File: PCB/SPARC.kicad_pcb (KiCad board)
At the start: 4 copper layers, 40 x 40 mm, 58 parts, among them J1 Conn_Coaxial_Power, J2 Conn_Coaxial_Power, J3 Conn_01x06_Female, J4 Conn_01x03_Female, J5 Conn_01x03_Female, J6 Conn_01x06_Female, U1 HV2621, U2 HV2621

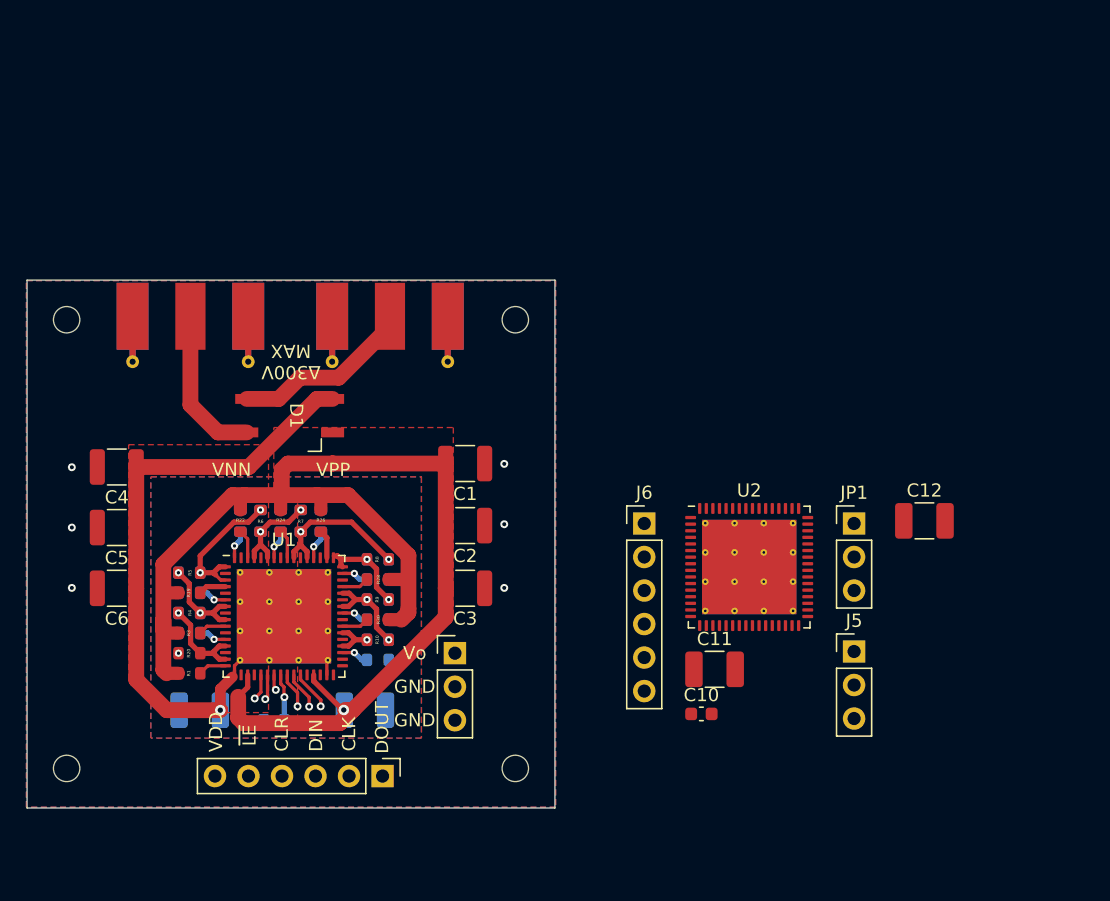
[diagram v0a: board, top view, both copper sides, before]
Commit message: Worked on adding second channel
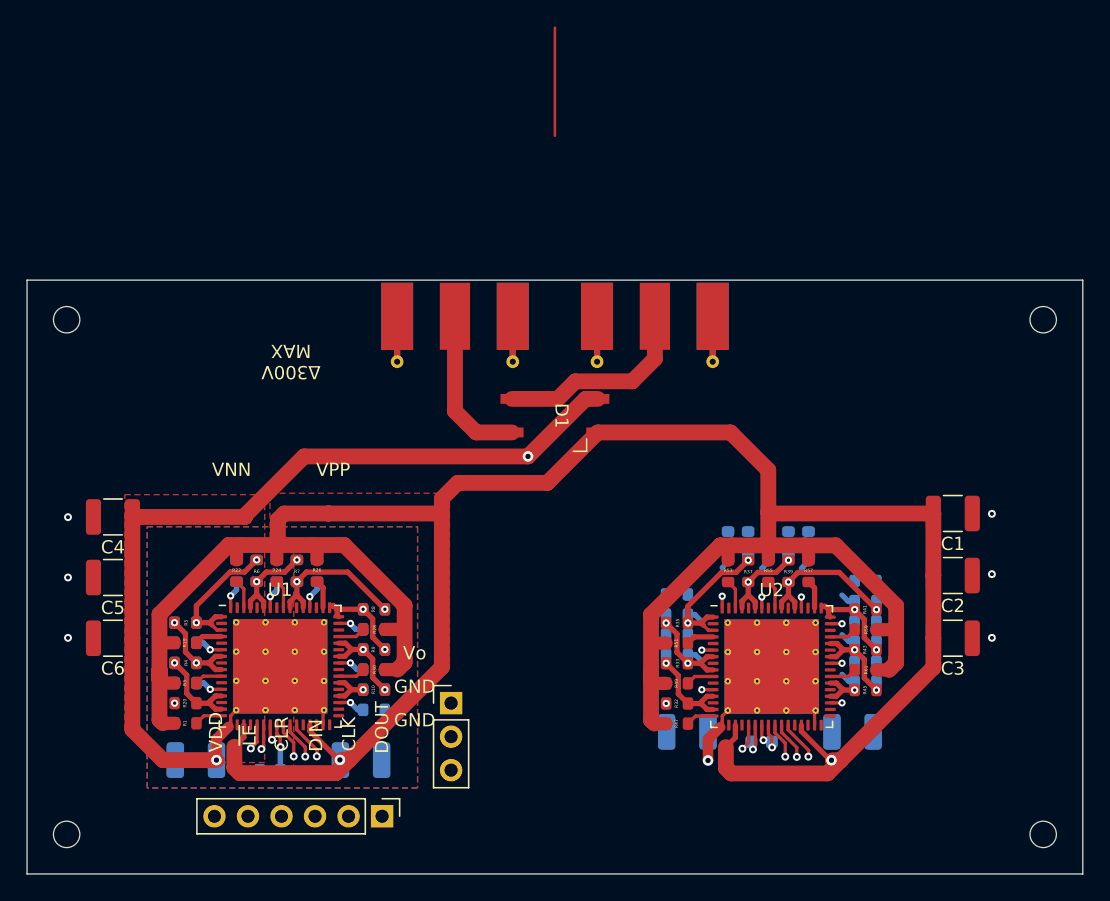
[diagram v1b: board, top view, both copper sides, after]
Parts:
- removed J5: Conn_01x03_Female, Connector_PinHeader_2.54mm:PinHeader_1x03_P2.54mm_Vertical
- removed J6: Conn_01x06_Female, Connector_PinHeader_2.54mm:PinHeader_1x06_P2.54mm_Vertical
- removed JP1: Jumper_3_Open, Connector_PinHeader_2.54mm:PinHeader_1x03_P2.54mm_Vertical
- added R32: ${2R}, grad_kicad_foot:R_0603_1608Metric_small_silk, F.Cu at (132.7, 76.7)
- added R33: ${2R}, grad_kicad_foot:R_0603_1608Metric_small_silk, F.Cu at (132.7, 73.7)
- added R34: ${2R}, grad_kicad_foot:R_0603_1608Metric_small_silk, B.Cu at (132.6, 71.5)
- added R35: ${2R}, grad_kicad_foot:R_0603_1608Metric_small_silk, F.Cu at (132.7, 70.6)
- added R36: ${2R}, grad_kicad_foot:R_0603_1608Metric_small_silk, B.Cu at (132.6, 68.4)
- added R37: ${2R}, grad_kicad_foot:R_0603_1608Metric_small_silk, F.Cu at (138.0, 66.7)
- added R38: ${2R}, grad_kicad_foot:R_0603_1608Metric_small_silk, B.Cu at (138.0, 64.5)
- added R39: ${2R}, grad_kicad_foot:R_0603_1608Metric_small_silk, F.Cu at (141.1, 66.7)
- added R40: ${2R}, grad_kicad_foot:R_0603_1608Metric_small_silk, B.Cu at (141.1, 64.5)
- added R41: ${2R}, grad_kicad_foot:R_0603_1608Metric_small_silk, F.Cu at (146.9, 69.6)
- added R42: ${2R}, grad_kicad_foot:R_0603_1608Metric_small_silk, B.Cu at (146.9, 67.4)
- added R43: ${2R}, grad_kicad_foot:R_0603_1608Metric_small_silk, F.Cu at (146.9, 72.6)
- added R44: ${2R}, grad_kicad_foot:R_0603_1608Metric_small_silk, B.Cu at (146.9, 70.5)
- added R45: ${2R}, grad_kicad_foot:R_0603_1608Metric_small_silk, F.Cu at (146.9, 75.7)
- added R46: ${2R}, grad_kicad_foot:R_0603_1608Metric_small_silk, B.Cu at (146.9, 73.5)
- added R47: ${2R}, grad_kicad_foot:R_0603_1608Metric_small_silk, F.Cu at (132.7, 78.2)
- added R48: ${2R}, grad_kicad_foot:R_0603_1608Metric_small_silk, B.Cu at (132.6, 73.0)
- added R49: ${2R}, grad_kicad_foot:R_0603_1608Metric_small_silk, F.Cu at (132.7, 75.2)
- added R50: ${2R}, grad_kicad_foot:R_0603_1608Metric_small_silk, B.Cu at (132.6, 70.0)
- added R51: ${2R}, grad_kicad_foot:R_0603_1608Metric_small_silk, F.Cu at (132.7, 72.1)
- added R52: ${2R}, grad_kicad_foot:R_0603_1608Metric_small_silk, B.Cu at (136.5, 64.5)
- added R53: ${2R}, grad_kicad_foot:R_0603_1608Metric_small_silk, F.Cu at (136.5, 66.7)
- added R54: ${2R}, grad_kicad_foot:R_0603_1608Metric_small_silk, B.Cu at (139.6, 64.5)
- added R55: ${2R}, grad_kicad_foot:R_0603_1608Metric_small_silk, F.Cu at (139.6, 66.7)
- added R56: ${2R}, grad_kicad_foot:R_0603_1608Metric_small_silk, B.Cu at (142.6, 64.5)
- added R57: ${2R}, grad_kicad_foot:R_0603_1608Metric_small_silk, F.Cu at (142.6, 66.7)
- added R58: ${2R}, grad_kicad_foot:R_0603_1608Metric_small_silk, B.Cu at (146.9, 69.0)
- added R59: ${2R}, grad_kicad_foot:R_0603_1608Metric_small_silk, F.Cu at (146.9, 71.1)
- added R60: ${2R}, grad_kicad_foot:R_0603_1608Metric_small_silk, B.Cu at (146.9, 72.0)
- added R61: ${2R}, grad_kicad_foot:R_0603_1608Metric_small_silk, F.Cu at (146.9, 74.2)
- added R62: ${2R}, grad_kicad_foot:R_0603_1608Metric_small_silk, B.Cu at (146.9, 75.0)
- C10, C11, C12: moved to B.Cu
- moved REF** 40.3 mm to (160.4, 86.6)
- moved REF** 40.0 mm to (160.4, 47.6)
- moved C1 37.1 mm to (153.6, 62.3)
- moved C2 37.1 mm to (153.6, 67.0)
- moved C3 37.1 mm to (153.6, 71.8)
- moved D1 20.1 mm to (123.4, 54.9)
- moved J2 20.1 mm to (131.0, 49.1)
- moved J1 20.0 mm to (115.8, 49.1)
- moved C12 16.9 mm to (146.0, 78.9), turned to 180 degrees
- moved U2 7.73 mm to (139.8, 73.9)
- moved C11 5.17 mm to (133.4, 78.9)
- moved C10 5.03 mm to (139.1, 79.6), turned to 180 degrees
- moved REF** 5.00 mm to (86.4, 86.6)
- moved C7 3.80 mm to (108.7, 81.0)
- moved C8 3.80 mm to (101.8, 81.8)
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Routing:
- net /VPP: track 99.2 -> 238.2 mm, vias 1 -> 2
- net /VNN: track 46.0 -> 105.5 mm, vias 1 -> 3
- net /VDD: track 18.9 -> 34.7 mm, vias 1 -> 2
- net /VB4_1: track 0.00 -> 11.5 mm, vias 0 -> 2
- net /VB2_1: track 0.00 -> 10.5 mm, vias 0 -> 2
- net /~{LE_0}: track 10.8 -> 19.4 mm
- net /VB0_1: track 0.00 -> 7.38 mm, vias 0 -> 1
- net /VB3_1: track 0.00 -> 7.11 mm, vias 0 -> 2
- net /VB7_0: track 10.3 -> 17.4 mm
- net /VB1_1: track 0.00 -> 7.02 mm, vias 0 -> 2
- net /VB6_1: track 0.00 -> 6.98 mm, vias 0 -> 2
- net /VB5_1: track 0.00 -> 6.93 mm, vias 0 -> 2
- net /DOUT_0: track 10.1 -> 16.9 mm
- net /CLR_0: track 8.72 -> 14.8 mm
- net /DIN_0: track 8.55 -> 13.8 mm
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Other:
- board size 40 x 40 mm -> 80 x 45 mm

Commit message: Changed resistors and added jumpers
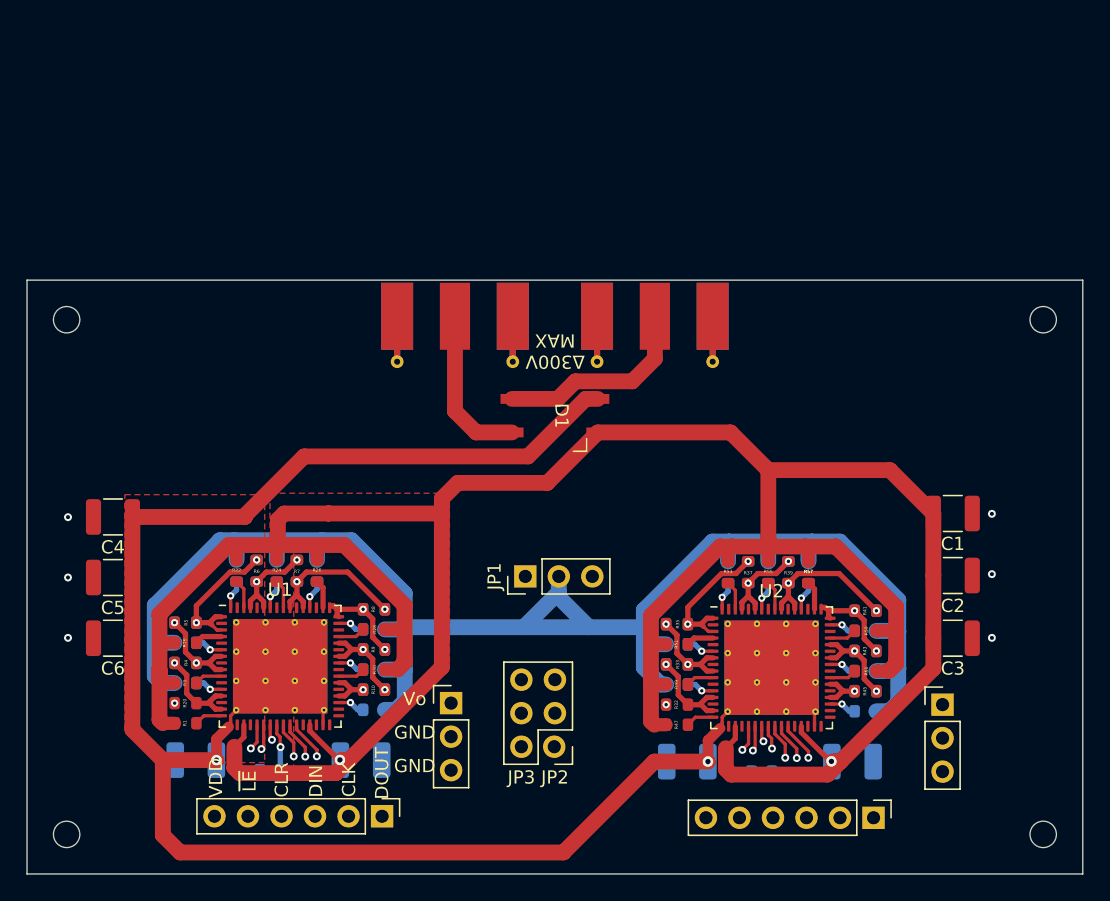
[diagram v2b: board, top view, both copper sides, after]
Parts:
- added J5: Conn_01x03_Female, Connector_PinHeader_2.54mm:PinHeader_1x03_P2.54mm_Vertical, F.Cu at (152.8, 76.8)
- added J6: Conn_01x06_Female, Connector_PinHeader_2.54mm:PinHeader_1x06_P2.54mm_Vertical, F.Cu at (147.5, 85.4)
- added JP1: Jumper_3_Open, Connector_PinHeader_2.54mm:PinHeader_1x03_P2.54mm_Vertical, F.Cu at (121.2, 67.1)
- added JP3 JP2: PinHeader_2x03_P2.54mm_Vertical, Connector_PinHeader_2.54mm:PinHeader_2x03_P2.54mm_Vertical, F.Cu at (123.4, 80.0)
- added R57: ${2R}, grad_kicad_foot:R_0603_1608Metric_small_silk, F.Cu at (142.6, 66.8)
- moved R46 2.25 mm to (146.9, 75.8)
- moved R62 2.25 mm to (146.9, 77.3)
- moved C10 2.25 mm to (139.1, 81.9)
- moved C11 2.25 mm to (133.4, 81.1)
- moved C12 2.25 mm to (146.0, 81.1)
- moved R34 2.25 mm to (132.6, 73.7)
- moved R36 2.25 mm to (132.6, 70.7)
- moved R38 2.25 mm to (138.0, 66.8)
- moved R40 2.25 mm to (141.1, 66.8)
- moved R42 2.25 mm to (146.9, 69.7)
- moved R44 2.25 mm to (146.9, 72.7)
- moved R48 2.25 mm to (132.6, 75.3)
- moved R50 2.25 mm to (132.6, 72.2)
- moved R52 2.25 mm to (136.5, 66.8)
- moved R54 2.25 mm to (139.6, 66.8)
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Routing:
- net /VL: track 0.00 -> 125.4 mm
- net /CLK_1: track 0.00 -> 20.1 mm
- net /VNN: track 105.5 -> 124.0 mm, vias 3 -> 2
- net /DIN_1: track 0.00 -> 13.7 mm
- net /~{LE_0}: track 19.4 -> 10.6 mm
- net /~{LE_1}: track 1.91 -> 10.7 mm
- net /VB7_0: track 17.4 -> 10.3 mm
- net /VB7_1: track 3.23 -> 10.3 mm
- net /DOUT_0: track 16.9 -> 9.86 mm
- net /DOUT_1: track 3.03 -> 9.86 mm
- net /CLR_0: track 14.8 -> 8.09 mm
- net /CLR_1: track 1.98 -> 8.09 mm
- net /DIN_0: track 13.8 -> 7.92 mm
- net /VPP: track 238.2 -> 233.2 mm
- removed copper zone on B.Cu, net GND
- removed copper zone on F.Cu, net GND
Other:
- board text removed: "VNN"
- board text removed: "VPP"

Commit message: Finished traces, finalized board
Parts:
- removed kibuzzard-63A22B4E: G***, kibuzzard-63A22B4E
- moved JP3 JP2 2.22 mm to (124.8, 81.7)
- moved JP1 0.52 mm to (120.9, 66.7)
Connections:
- JP3 JP2 pad 1: /CLK_1 -> /DIN_1
- JP3 JP2 pad 2: /DIN_1 -> /CLK_1
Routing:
- net /VDD: track 35.2 -> 76.2 mm
- net /SRi_1: track 2.71 -> 34.9 mm
- net /CLK_0: track 8.77 -> 38.5 mm
- net /SRc_1: track 2.89 -> 23.2 mm
- net /DOUT_0: track 9.86 -> 28.9 mm
- net /VNN: track 124.0 -> 134.6 mm, vias 2 -> 3
- net /DIN_1: track 13.7 -> 22.5 mm
- net /CLK_1: track 20.1 -> 28.1 mm
- net /VL: track 125.4 -> 121.2 mm
- added copper zone on B.Cu, net /VL
- added copper zone on B.Cu, net GND
- added copper zone on F.Cu, net GND
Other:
- board text added: "2CH-HV-DAC"
- board text added: "Daisy-Chain"
- board text added: "Independent"
- board text added: "Original 1CH Design: Randy Palamar 2023 <palamar@ualberta.ca> 2CH Design: Kirk Rieberger 2023 <rieberg1@ualberta.ca>"
- board text added: "VPP/GND"
- board text added: "VPP/VNN"
- board text removed: "Randy Palamar 2023 <palamar@ualberta.ca>"

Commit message: Updated R20 & R32 connection
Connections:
- R20 pad 2: GND -> /VL
- R32 pad 2: GND -> /VL
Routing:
- net GND: vias 10 -> 8
- net /VL: vias 0 -> 2
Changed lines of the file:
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@@
       (net 55 "/VB0_0") (pintype "passive"))
     (pad "2" smd roundrect (at 0.825 0 180) (size 0.8 0.95) (layers "F.Cu" "F.Paste" "F.Mask") (roundrect_rratio 0.25)
-      (net 7 "GND") (pintype "passive"))
+      (net 54 "/VL") (pintype "passive"))
     (model "${KICAD6_3DMODEL_DIR}/Resistor_SMD.3dshapes/R_0603_1608Metric.wrl"
       (offset (xyz 0 0 0))
@@
       (net 72 "/VB0_1") (pintype "passive"))
     (pad "2" smd roundrect (at 0.825 0 180) (size 0.8 0.95) (layers "F.Cu" "F.Paste" "F.Mask") (roundrect_rratio 0.25)
-      (net 7 "GND") (pintype "passive"))
+      (net 54 "/VL") (pintype "passive"))
     (model "${KICAD6_3DMODEL_DIR}/Resistor_SMD.3dshapes/R_0603_1608Metric.wrl"
       (offset (xyz 0 0 0))
@@
   (gr_line (start 127 79.3) (end 127 82.5) (layer "F.SilkS") (width 0.2))
   (gr_line (start 123.1 64.5) (end 126.3 64.5) (layer "F.SilkS") (width 0.2))
-  (gr_rect (start 92.784 59.478769) (end 113.359 79.378769) (layer "Dwgs.User") (width 0.2) (fill none))
+  (gr_rect (start 83.43 44.61) (end 163.399 89.64) (layer "Dwgs.User") (width 0.2) (fill none))
   (gr_rect (start 83.4 44.628769) (end 163.4 89.628769) (layer "Edge.Cuts") (width 0.1) (fill none))
   (gr_text "2CH-HV-DAC" (at 99.1 47.8) (layer "B.SilkS")
@@
   (via (at 86.502682 71.735369) (size 0.6) (drill 0.3) (layers "F.Cu" "B.Cu") (free) (net 7))
   (via (at 156.513682 71.735369) (size 0.6) (drill 0.3) (layers "F.Cu" "B.Cu") (free) (net 7))
-  (via (at 131.827682 76.796) (size 0.55) (drill 0.25) (layers "F.Cu" "B.Cu") (net 7))
   (via (at 86.502682 67.163369) (size 0.6) (drill 0.3) (layers "F.Cu" "B.Cu") (free) (net 7))
   (via (at 156.513682 62.337369) (size 0.6) (drill 0.3) (layers "F.Cu" "B.Cu") (free) (net 7))
@@
   (via (at 156.513682 66.909369) (size 0.6) (drill 0.3) (layers "F.Cu" "B.Cu") (free) (net 7))
   (via (at 86.502682 62.591369) (size 0.6) (drill 0.3) (layers "F.Cu" "B.Cu") (free) (net 7))
-  (via (at 94.583682 76.6846) (size 0.55) (drill 0.25) (layers "F.Cu" "B.Cu") (net 7))
   (via (at 139.202682 79.574769) (size 0.6) (drill 0.3) (layers "F.Cu" "B.Cu") (free) (net 7))
   (segment (start 102.828682 78.3261) (end 102.828682 78.9046) (width 0.25) (layer "F.Cu") (net 8))
@@
   (segment (start 99.828682 69.4511) (end 99.828682 68.0306) (width 0.25) (layer "F.Cu") (net 53))
   (segment (start 99.828682 68.0306) (end 99.276682 67.4786) (width 0.25) (layer "F.Cu") (net 53))
+  (via (at 131.827682 76.796) (size 0.55) (drill 0.25) (layers "F.Cu" "B.Cu") (net 54))
+  (via (at 94.583682 76.6846) (size 0.55) (drill 0.25) (layers "F.Cu" "B.Cu") (net 54))
   (segment (start 130.14 73.98) (end 131.43 75.27) (width 1.2) (layer "B.Cu") (net 54))
   (segment (start 112.02 76.53) (end 111.3594 77.1906) (width 1.2) (layer "B.Cu") (net 54))
@@
         (xy 148.5 77.9)
         (xy 134.7 77.9)
-        (xy 132.2 75.9)
-        (xy 113.3 75.9)
-        (xy 111.985623 77.740574)
-        (xy 97.2 77.7)
-        (xy 94.654868 75.876991)
-        (xy 93.3 75.6)
-        (xy 93.1 69.2)
+        (xy 132.18 77.9)
+        (xy 113.25 77.9)
+        (xy 112.01 77.9)
+        (xy 97.15 77.9)
+        (xy 92.49 77.9)
+        (xy 92.46 75.59)
+        (xy 92.489816 69.100062)
         (xy 98.1 64.3)
         (xy 108.1 64.3)

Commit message: Reworked mode select jumpers
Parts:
- added JP3 JP2: PinHeader_2x03_P2.54mm_Vertical, Connector_PinHeader_2.54mm:PinHeader_2x03_P2.54mm_Vertical, F.Cu at (128.1, 81.7)
- moved JP3 JP2 3.00 mm to (121.8, 81.7)
- moved JP1 1.98 mm to (120.9, 64.7)
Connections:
- JP3 JP2 pad 3: /SRc_1 -> /SRdin_1
- JP3 JP2 pad 4: /SRi_1 -> /SRclk_1
- JP3 JP2 pad 5: /CLK_0 -> /DOUT_0
- JP3 JP2 pad 6: /DOUT_0 -> /CLK_0
- U2 pad 21: /CLR_1 -> /SRclr_1
- U2 pad 22: /~{LE_1} -> /~{SRle_1}
- U2 pad 25: /SRi_1 -> /SRdin_1
- U2 pad 26: /SRc_1 -> /SRclk_1
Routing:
- net /CLR_0: track 8.09 -> 43.9 mm
- net /SRi_1: track 34.9 -> 0.00 mm, vias 1 -> 0
- net /~{LE_0}: track 10.6 -> 44.9 mm
- net /SRclk_1: track 0.00 -> 30.7 mm, vias 0 -> 1
- net /SRdin_1: track 0.00 -> 26.9 mm, vias 0 -> 1
- net /VDD: track 76.2 -> 101.4 mm
- net /SRc_1: track 23.2 -> 0.00 mm, vias 1 -> 0
- net /~{SRle_1}: track 0.00 -> 17.3 mm, vias 0 -> 1
- net /SRclr_1: track 0.00 -> 11.9 mm, vias 0 -> 1
- net /CLR_1: track 8.09 -> 13.4 mm, vias 1 -> 0
- net /DIN_1: track 22.5 -> 26.6 mm
- net /CLK_1: track 28.1 -> 31.8 mm
- net /~{LE_1}: track 10.7 -> 14.3 mm, vias 1 -> 0
- net /VL: track 121.2 -> 123.2 mm
- net /VNN: track 134.6 -> 132.7 mm
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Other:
- board text added: "Jumpers Down: Independent Channels"
- board text added: "Jumpers Up: Daisy Chain Channels"
- board text added: "Low Voltage Select"
- board text added: "Mode Select"
- board text added: "Mode Select Instructions: ~{ ALL JUMPERS MUST BE } IN THE SAME POSITION"
- board text removed: "Daisy-Chain"
- board text removed: "Independent"

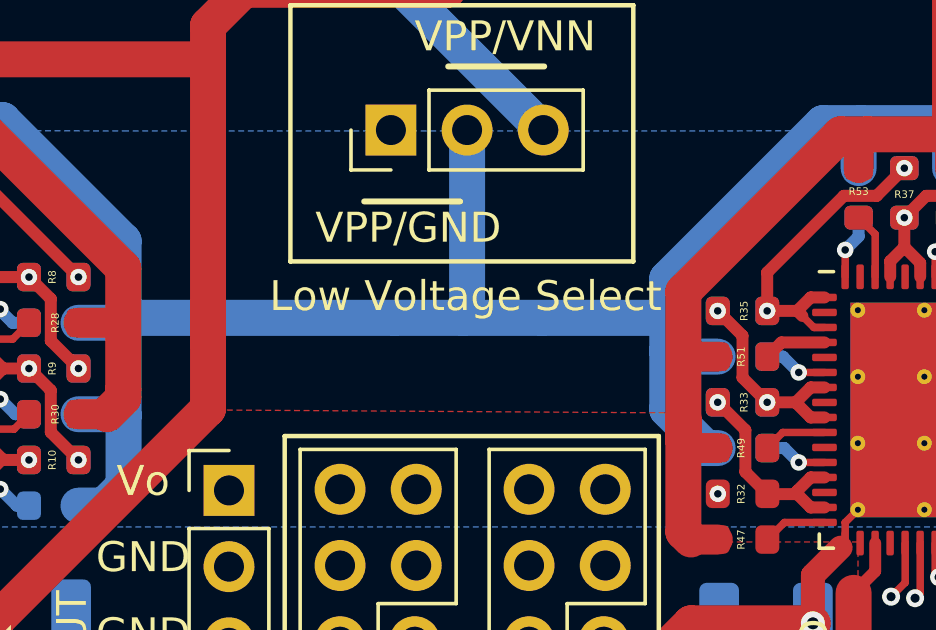
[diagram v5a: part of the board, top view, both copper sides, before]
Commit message: Updated BOM to optimize costs
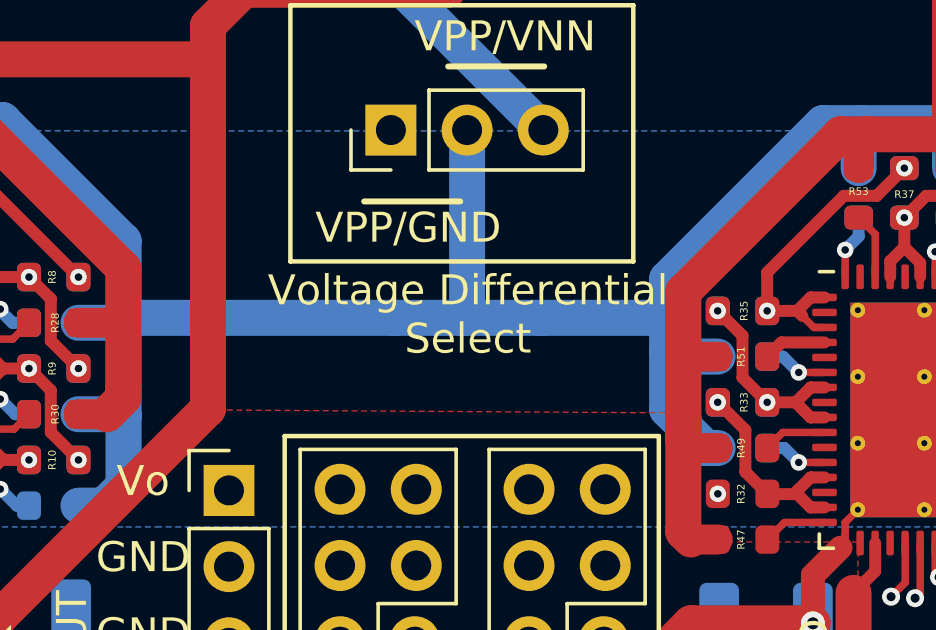
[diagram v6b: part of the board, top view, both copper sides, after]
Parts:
- JP4 JP5: renamed from JP3 JP2
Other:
- board text added: "Voltage Differential Select"
- board text removed: "Low Voltage Select"
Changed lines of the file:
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@@
     (tags "Through hole pin header THT 2x03 2.54mm double row")
     (attr through_hole)
-    (fp_text reference "JP3 JP2" (at 1.275 -2.475) (layer "F.SilkS") hide
+    (fp_text reference "JP4 JP5" (at 1.275 -2.475) (layer "F.SilkS") hide
       (effects (font (size 1 1) (thickness 0.15)))
     )
@@
     (effects (font (size 1 1) (thickness 0.15)))
   )
-  (gr_text "Low Voltage Select" (at 123.42 70.21) (layer "F.SilkS")
-    (effects (font (size 1 1) (thickness 0.15)))
-  )
+  (gr_text "Voltage Differential\nSelect" (at 123.5 70.82) (layer "F.SilkS")
+    (effects (font (size 1 1) (thickness 0.15)))
+  )
